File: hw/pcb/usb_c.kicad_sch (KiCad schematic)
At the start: 25 parts, among them J1 USB_C_Receptacle, U1 MUN12AD01-SH, U2 HD3SS3220, U3 MG2040

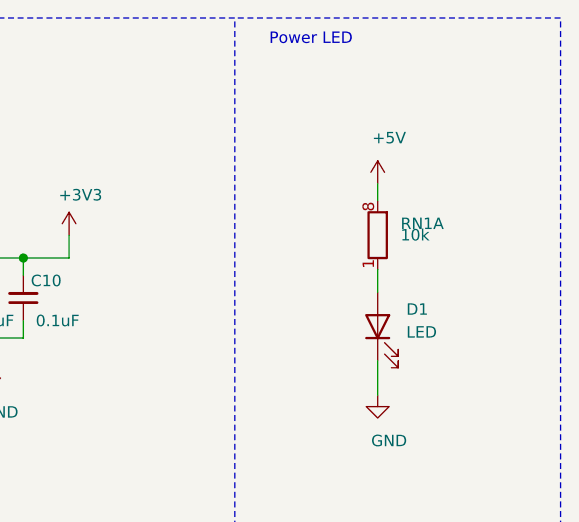
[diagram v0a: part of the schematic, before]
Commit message: whisperbounce: assign footprints
Signed-off-by: Dominik Sliwa <dominik@sliwa.io>
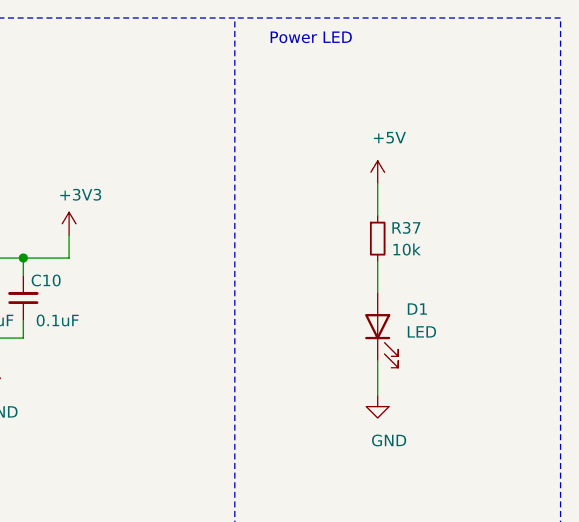
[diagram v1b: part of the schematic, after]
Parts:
- removed RN1: 10k, Resistor_SMD:R_Array_Convex_4x0402, symbol Device:R_Pack04_Split
- added R37: 10k, Resistor_SMD:R_0402_1005Metric, symbol Device:R_Small
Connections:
- net +5V: now also R37.1
- net at D1.2 (A): now also R37.2
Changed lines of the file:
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@@
   (junction (at 160.02 47.625) (diameter 1.016) (color 0 0 0 0))
   (junction (at 163.83 38.735) (diameter 1.016) (color 0 0 0 0))
+  (no_connect (at 135.255 128.905))
+  (no_connect (at 135.255 146.685))
+  (no_connect (at 135.255 151.765))
+  (no_connect (at 48.895 141.605))
+  (no_connect (at 135.255 126.365))
+  (no_connect (at 119.38 43.815))
+  (no_connect (at 135.255 141.605))
+  (no_connect (at 139.7 43.815))
   (no_connect (at 135.255 154.305))
   (no_connect (at 135.255 144.145))
-  (no_connect (at 135.255 151.765))
-  (no_connect (at 135.255 128.905))
-  (no_connect (at 48.895 141.605))
-  (no_connect (at 135.255 141.605))
-  (no_connect (at 135.255 146.685))
-  (no_connect (at 119.38 43.815))
   (no_connect (at 48.895 139.065))
-  (no_connect (at 135.255 126.365))
-  (no_connect (at 139.7 43.815))
   (wire (pts (xy 26.035 151.13) (xy 26.035 149.225))
     (stroke (width 0) (type solid) (color 0 0 0 0))
@@
     (stroke (width 0) (type solid) (color 0 0 0 0))
   )
-  (wire (pts (xy 203.2 30.48) (xy 203.2 32.385))
-    (stroke (width 0) (type solid) (color 0 0 0 0))
-  )
-  (wire (pts (xy 203.2 40.005) (xy 203.2 42.545))
+  (wire (pts (xy 203.2 30.48) (xy 203.2 34.036))
+    (stroke (width 0) (type solid) (color 0 0 0 0))
+  )
+  (wire (pts (xy 203.2 39.116) (xy 203.2 42.545))
     (stroke (width 0) (type solid) (color 0 0 0 0))
   )
@@
     )
   )
+  (symbol (lib_id "Device:R_Small") (at 203.2 36.576 0) (unit 1)
+    (in_bom yes) (on_board yes)
+    (property "Reference" "R37" (id 0) (at 206.375 35.433 0))
+    (property "Value" "10k" (id 1) (at 206.375 37.846 0))
+    (property "Footprint" "Resistor_SMD:R_0402_1005Metric" (id 2) (at 203.2 36.576 0)
+      (effects (font (size 1.27 1.27)) hide)
+    )
+    (property "Datasheet" "~" (id 3) (at 203.2 36.576 0)
+      (effects (font (size 1.27 1.27)) hide)
+    )
+  )
   (symbol (lib_id "Device:C_Small") (at 68.58 113.665 90) (unit 1)
     (in_bom yes) (on_board yes)
@@
       (effects (font (size 1.27 1.27)) hide)
     )
-  )
-  (symbol (lib_id "Device:R_Pack04_Split") (at 203.2 36.195 0) (unit 1)
-    (in_bom yes) (on_board yes)
-    (property "Reference" "RN1" (id 0) (at 205.74 34.925 0)
-      (effects (font (size 1.27 1.27)) (justify left))
-    )
-    (property "Value" "10k" (id 1) (at 205.74 36.195 0)
-      (effects (font (size 1.27 1.27)) (justify left))
-    )
-    (property "Footprint" "Resistor_SMD:R_Array_Convex_4x0402" (id 2) (at 201.168 36.195 90)
-      (effects (font (size 1.27 1.27)) hide)
-    )
-    (property "Datasheet" "~" (id 3) (at 203.2 36.195 0)
-      (effects (font (size 1.27 1.27)) hide)
-    )

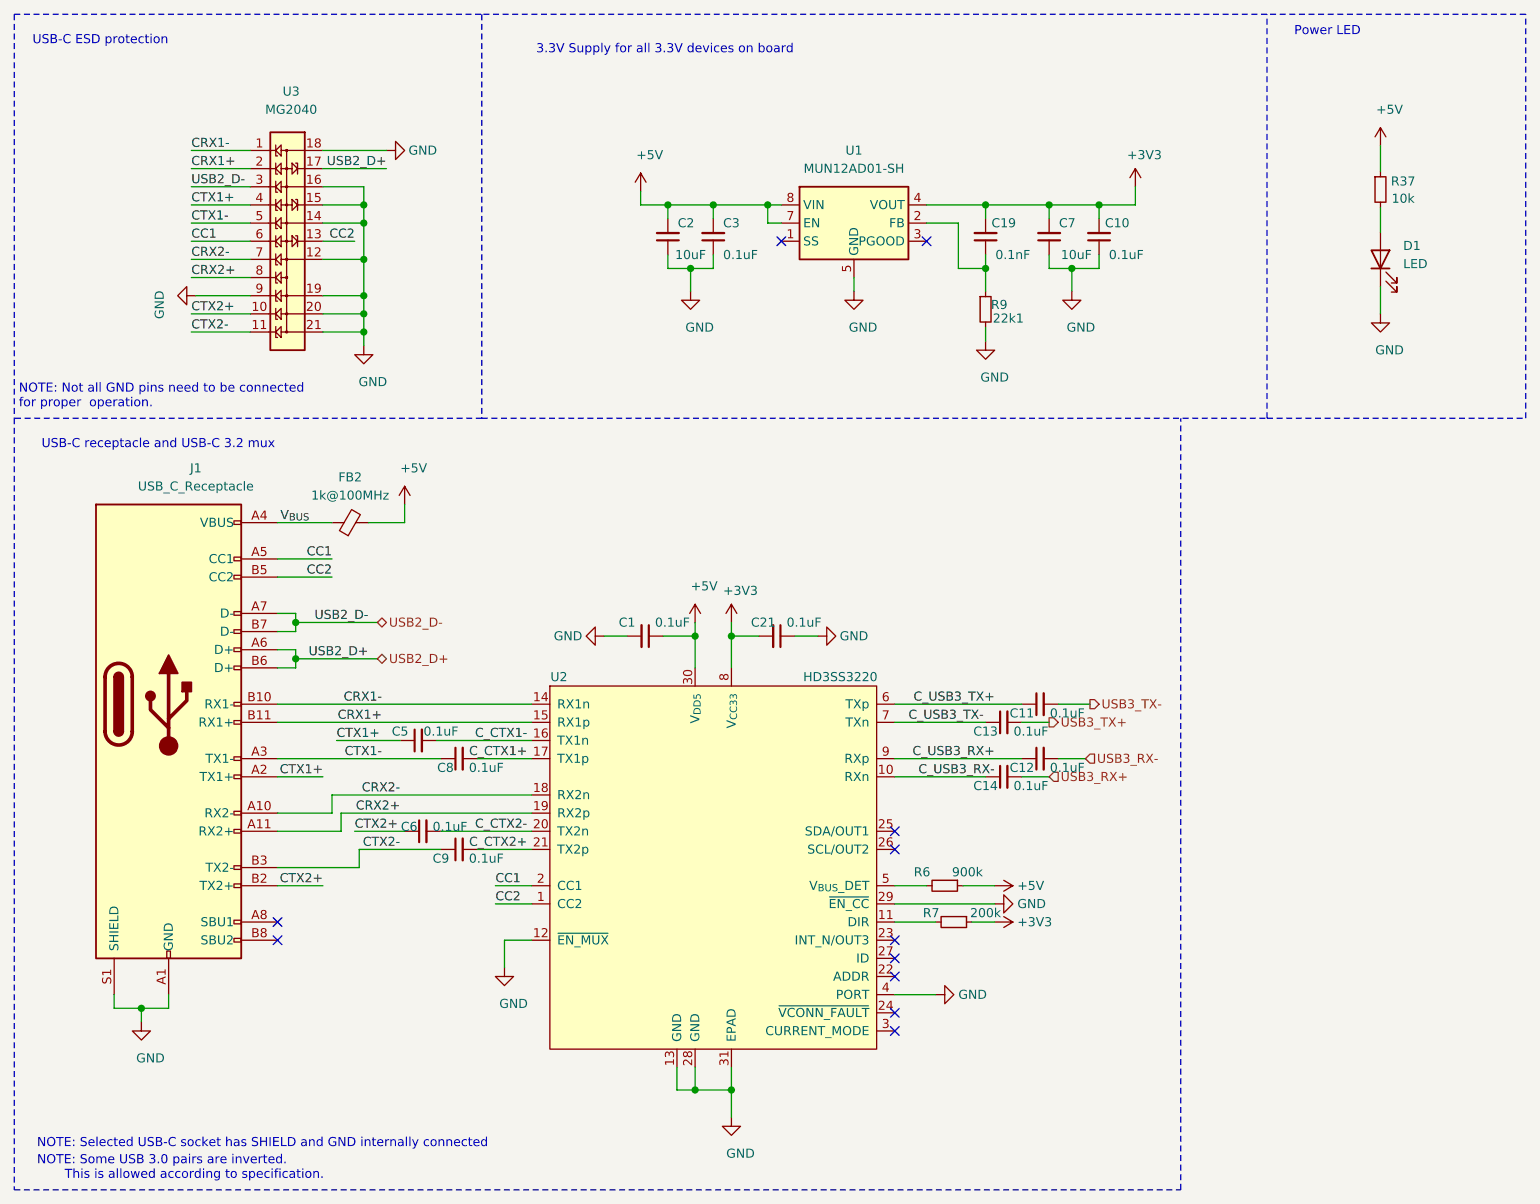
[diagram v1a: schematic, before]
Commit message: whisperbounce: pcb v1
Includes schematic and assigment tweaks

Signed-off-by: Dominik Sliwa <dominik@sliwa.io>
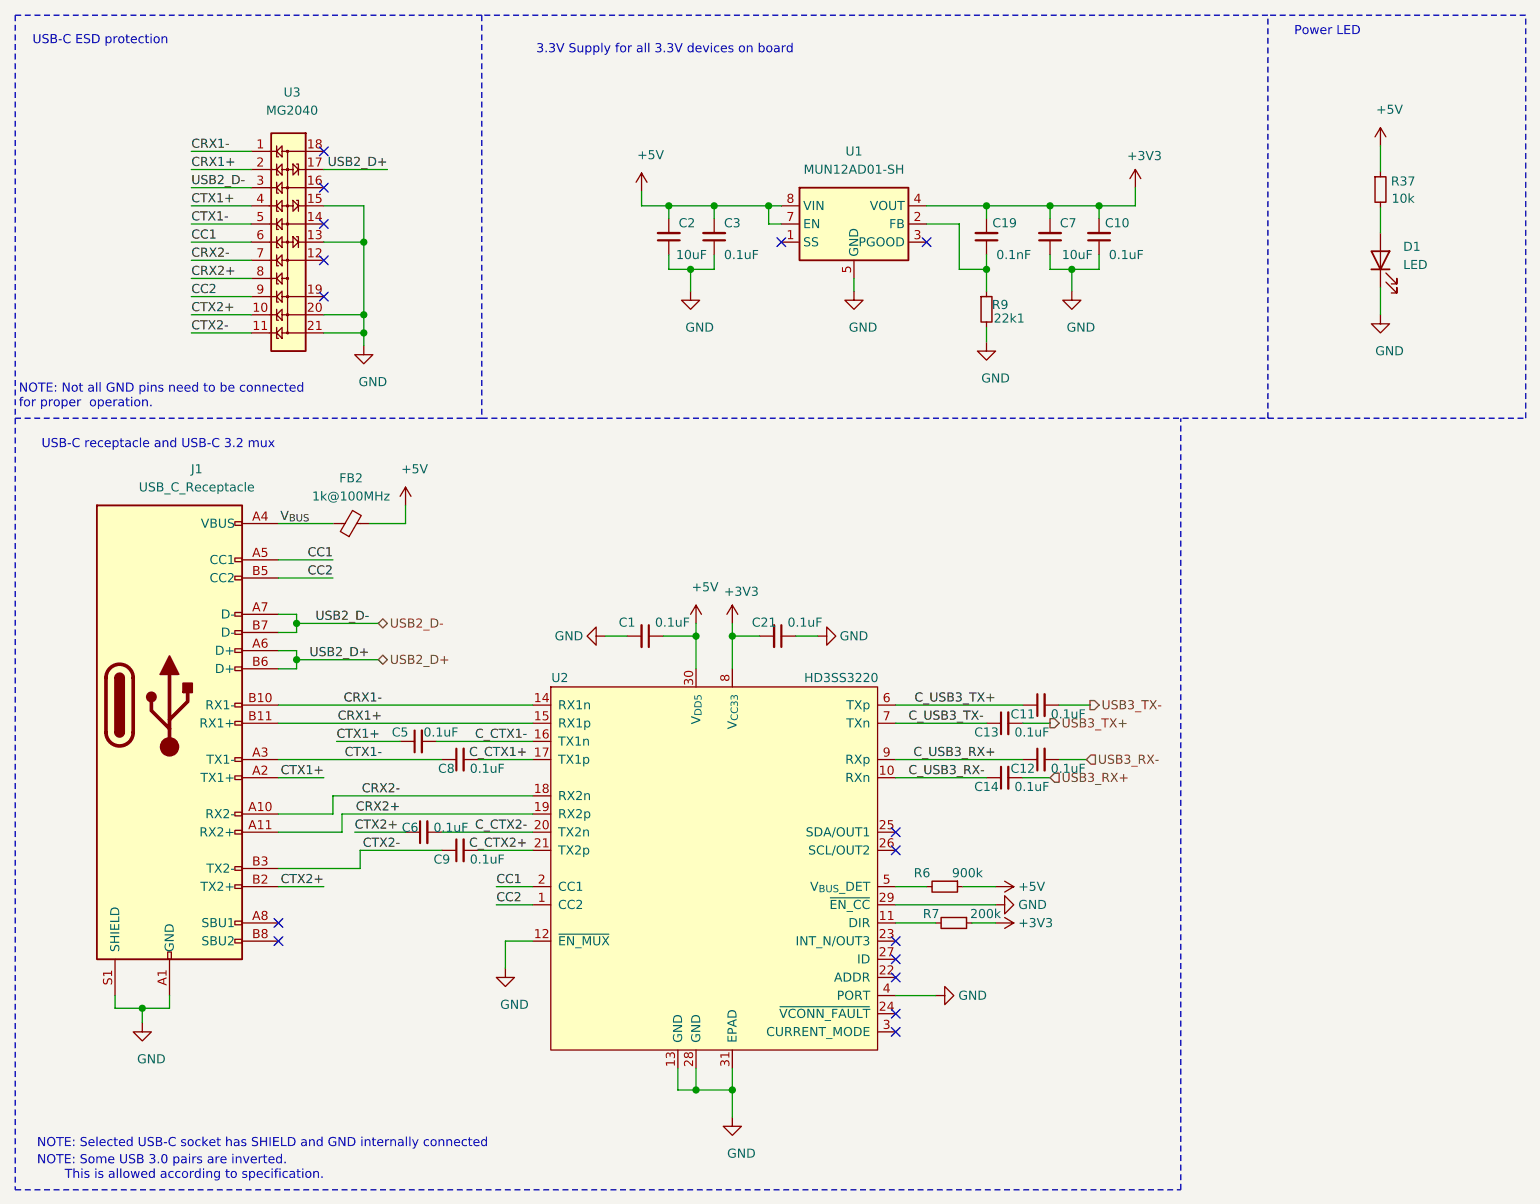
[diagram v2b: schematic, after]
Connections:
- net CC2: now also U3.9; no longer U3.13
- net C_USB3_RX-: now also C14.1, U2.10 (RXn)
- net GND: now also U3.13; no longer U3.12, U3.14, U3.16, U3.18, U3.19, U3.9
- no-connect marks 11 -> 16
